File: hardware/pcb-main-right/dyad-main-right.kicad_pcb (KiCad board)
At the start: 2 copper layers, 167.2 x 120.7 mm, 148 parts, among them SW1 SW_Push, SW10 SW_Push, SW11 SW_Push, SW12 SW_Push, SW13 SW_Push, SW14 SW_Push, SW15 SW_Push, SW16 SW_Push, SW17 SW_Push, SW18 SW_Push, SW19 SW_Push, SW2 SW_Push, SW20 SW_Push, SW21 SW_Push, SW22 SW_Push, SW23 SW_Push, SW24 SW_Push, SW25 SW_Push, SW26 SW_Push, SW27 SW_Push, SW28 SW_Push, SW29 SW_Push, SW3 SW_Push, SW30 SW_Push, SW31 SW_Push, SW32 SW_Push, SW33 SW_Push, SW34 SW_Push, SW35 SW_Push, SW36 SW_Push, SW37 SW_Push, SW4 SW_Push, SW5 SW_Push, SW6 SW_Push, SW7 SW_Push, SW8 SW_Push, SW9 SW_Push

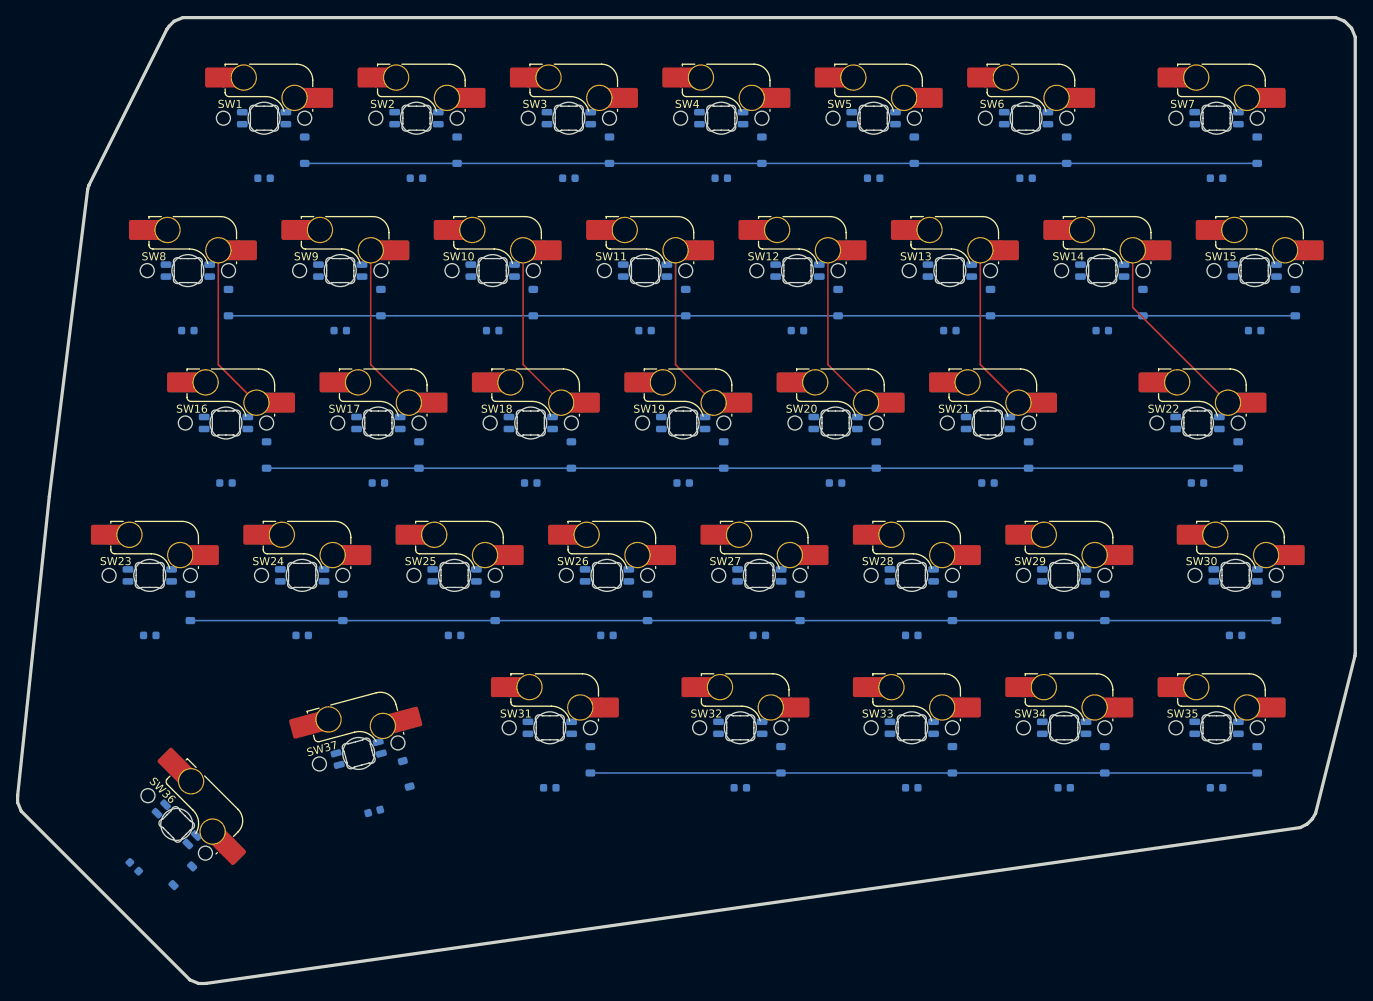
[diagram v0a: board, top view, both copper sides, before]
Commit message: Place switches on the back so hotswap sockets are on the underside
Caught in review: the sockets were on the same side as the switches.

marbastlib's hotswap footprint carries its socket pads on F.Cu and draws
its pin holes mirrored -- it is drawn as seen from underneath and must be
placed on the back. kbplacer defaults to front, so the sockets landed on
the switch side. Fixed with -s "SW{} 0 BACK"; stabilizers follow (they are
purely mechanical NPTH and X-symmetric, so flipping is a no-op for them).

Now every component is on the underside and switches insert from the top,
as a hotswap board should be. Verified: SW1's hotswap SMD pads are on
B.Cu, and the pin1->pin2 vector is (-6.35, 2.54), matching KiCad's stock
SW_Cherry_MX_1.00u_PCB. Absolute pad coordinates are not comparable
between the two libraries -- marbastlib's origin is the switch centre,
KiCad's is pin 1 -- so the vector is the valid test. An earlier claim in
this session that the geometry was mirrored wrongly was based on that bad
comparison and was itself wrong.

Also drops switch-to-diode routing failures, which were "no common layers
found" precisely because front-only SMD pads could not reach back-side
diodes.

DRC now runs and the boards are clearly a placement scaffold, not a
finished layout. Left: 1151 violations, 220 unconnected. Specific causes,
for the next pass:

- 128 hole_clearance: LEDs sit at the switch centre, 0.121 mm from the MX
  centre-post NPTH. The centre is where marbastlib puts its own combined
  MX+WS2812 footprint, but SK6812MINI-E is larger and fouls the post. LED
  offset needs rework.
- 128 copper_edge_clearance: the reverse-mount LED footprint's own cutout
  sits 0.35 mm from its pads against a 0.5 mm board rule. A board-setup
  constraint to relax, not a placement error.
- 192 shorting_items: diode pads overlapping switch through-holes after
  the flip, plus hotswap SMD pads left with no net, which points at an
  incomplete schematic-to-PCB netlist sync.
- Silk overlaps a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
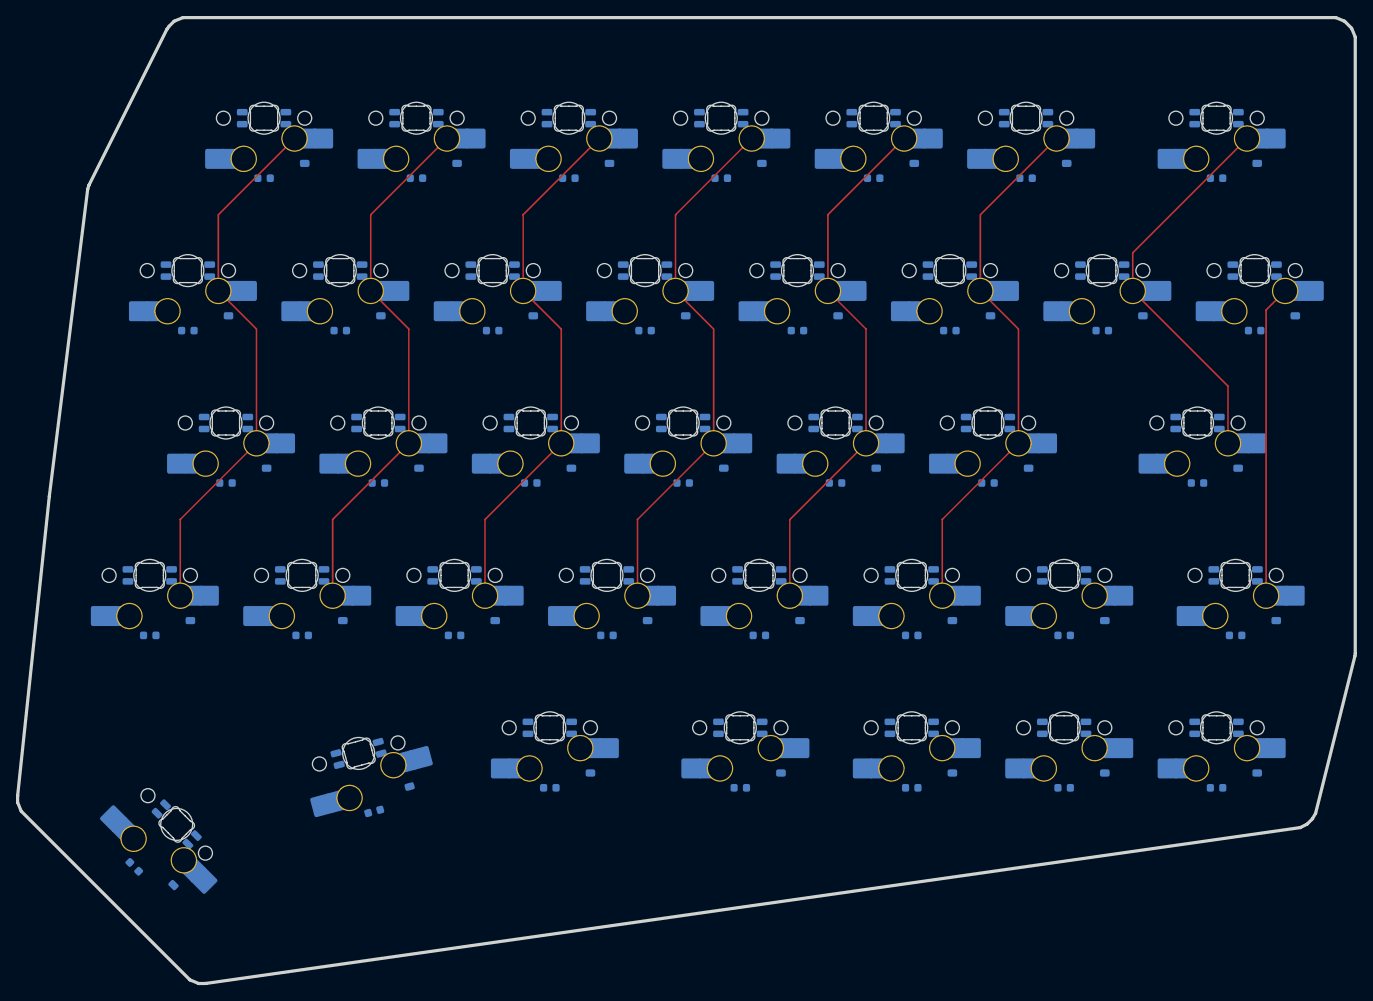
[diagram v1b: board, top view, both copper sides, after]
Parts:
- SW1, SW10, SW11, SW12, SW13, SW14, SW15, SW16, SW17, SW18, SW19, SW2, SW20, SW21, SW22, SW23, SW24, SW25, SW26, SW27, SW28, SW29, SW3, SW30, SW31, SW32, SW33, SW34, SW35, SW36, SW37, SW4, SW5, SW6, SW7, SW8, SW9: moved to B.Cu
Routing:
- net ROW3: track 135.7 -> 0.00 mm
- net ROW1: track 133.4 -> 0.00 mm
- net ROW2: track 121.4 -> 0.00 mm
- net ROW0: track 119.1 -> 0.00 mm
- net ROW4: track 83.3 -> 0.00 mm
- net COL4: track 21.0 -> 67.0 mm
- net COL3: track 21.0 -> 67.0 mm
- net COL2: track 21.0 -> 67.0 mm
- net COL1: track 21.0 -> 67.0 mm
- net COL0: track 21.0 -> 67.0 mm
- net COL5: track 21.0 -> 67.0 mm
- net COL7: track 0.00 -> 39.1 mm
- net COL6: track 24.0 -> 48.9 mm

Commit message: Fix LED offset and the placement errors it exposed
Working out the LED position turned up three further placement bugs.
Left board: 1151 -> 581 DRC violations, 220 -> 188 unconnected.

LED offset. ebastler's MX_SK6812MINI-E add-on -- a rear-mount SK6812MINI-E
for regular MX footprints -- puts its pads at y 4.33/5.83, centroid
(0, +5.08): 5.08 mm south of the switch centre, one fifth of an inch. Its
pad geometry matches KiCad's stock ReverseMount footprint almost exactly
(x +-2.6 vs +-2.73, same +-0.75 in y), so the maintained stock footprint
drops in at that offset. At the switch centre it fouled the MX centre-post
hole by 0.12 mm.

Switch rotation. The switches were 180 deg from convention: pins landed
SOUTH of centre, exactly where the LED goes. KiCad's stock MX footprint
puts them NORTH, at (+2.54,-5.08) and (-3.81,-2.54) relative to the
centre-post NPTH. An earlier commit asserted the geometry was correct on
the strength of the pin1->pin2 vector; that test cannot see this, because
a 180 deg rotation with swapped pin numbering preserves the vector.

Diode. kbplacer's default position assumes an unrotated switch, so it sat
beside the COLUMN pin, which the schematic does not wire it to. Moved
beside switch pin 2 and turned 180 deg so the anode rather than the ROW
pad faces the switch -- the ROW pad had been 0.035 mm from it.

Pad nets. marbastlib's hotswap footprint carries pad "1" three times, one
PTH and two SMD. kbplacer nets only one, so DRC saw each switch shorting
itself, 128 times per board. The generator now propagates nets across
same-numbered pads.

Also: min_copper_edge_clearance to 0.2 mm, since the reverse-mount LED
footprint's own light cutout sits 0.247 mm from its pads. Applied after
the board save, because saving rewrites the project file and silently
reverted it the first time.

Remaining, for a manual pass: roughly half the count is silkscreen
cosmetics and lib_footprint_issues (the libraries are referenced by
absolute path, so KiCad reports them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
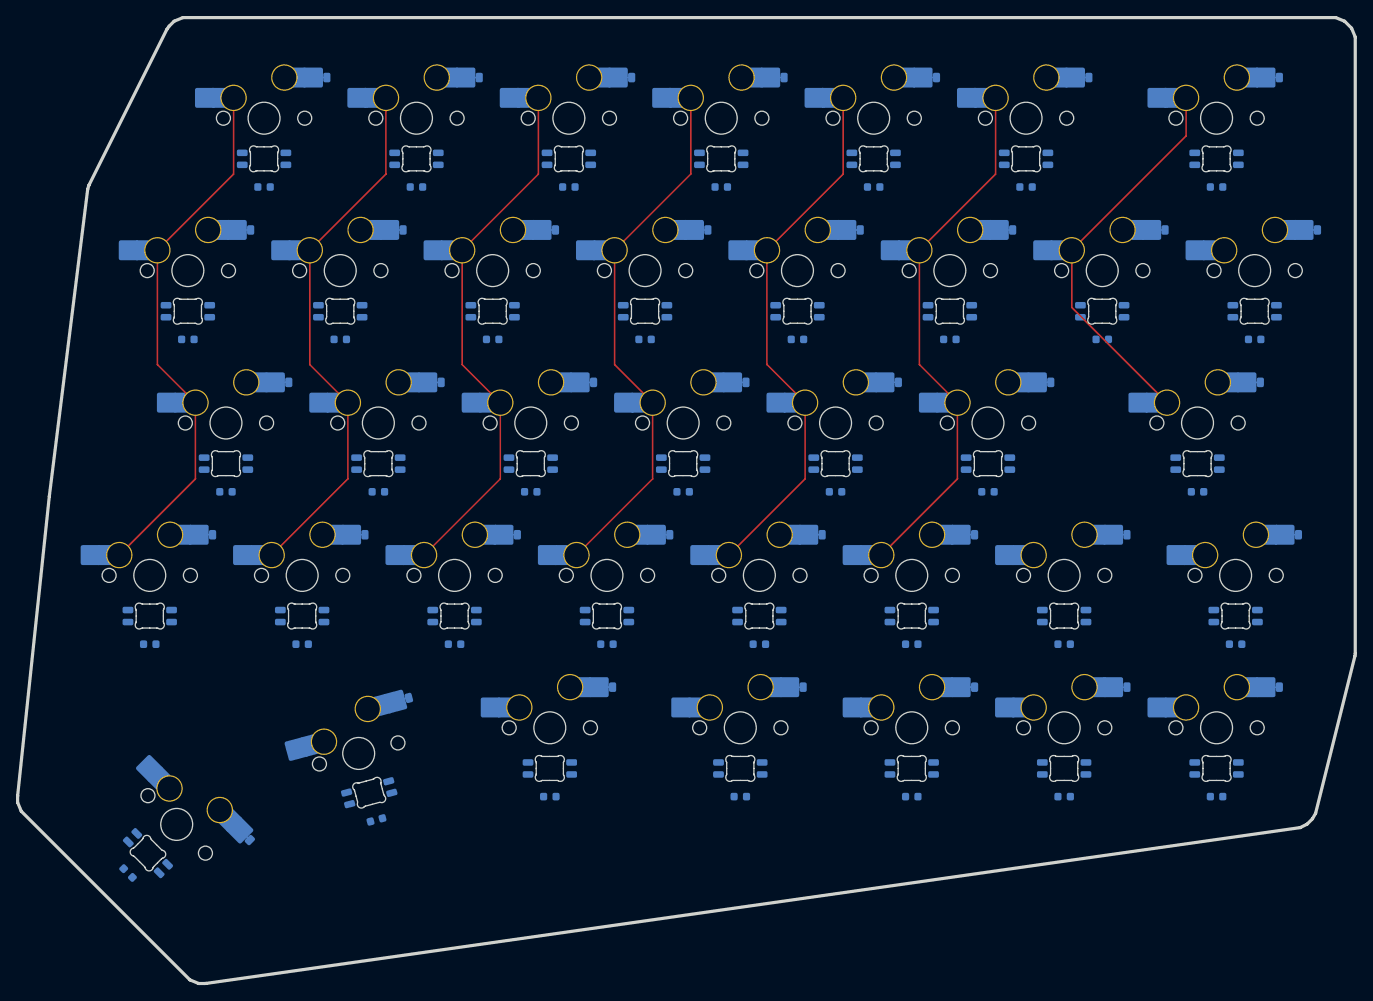
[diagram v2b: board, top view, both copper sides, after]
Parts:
- moved D36 9.15 mm to (54.2, 127.2), turned to -45 degrees
- moved D37 9.15 mm to (73.7, 111.0), turned to 15 degrees
- moved D1 9.15 mm to (63.4, 33.0), turned to 0 degrees
- moved D10 9.15 mm to (91.9, 52.1), turned to 0 degrees
- moved D11 9.15 mm to (111.0, 52.1), turned to 0 degrees
- moved D12 9.15 mm to (130.0, 52.1), turned to 0 degrees
- moved D14 9.15 mm to (168.1, 52.1), turned to 0 degrees
- moved D15 9.15 mm to (187.2, 52.1), turned to 0 degrees
- moved D16 9.15 mm to (58.6, 71.1), turned to 0 degrees
- moved D17 9.15 mm to (77.6, 71.1), turned to 0 degrees
- moved D18 9.15 mm to (96.7, 71.1), turned to 0 degrees
- moved D19 9.15 mm to (115.7, 71.1), turned to 0 degrees
- moved D2 9.15 mm to (82.4, 33.0), turned to 0 degrees
- moved D20 9.15 mm to (134.8, 71.1), turned to 0 degrees
- moved D21 9.15 mm to (153.8, 71.1), turned to 0 degrees
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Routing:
- net COL7: track 39.1 -> 0.00 mm
- net Net-(D33-A): track 0.00 -> 1.76 mm
- net Net-(D28-A): track 0.00 -> 1.76 mm
- net Net-(D22-A): track 0.00 -> 1.76 mm
- net Net-(D21-A): track 0.00 -> 1.76 mm
- net Net-(D14-A): track 0.00 -> 1.76 mm
- net Net-(D12-A): track 0.00 -> 1.76 mm
- net Net-(D32-A): track 0.00 -> 1.76 mm
- net Net-(D31-A): track 0.00 -> 1.76 mm
- net Net-(D25-A): track 0.00 -> 1.76 mm
- net Net-(D24-A): track 0.00 -> 1.76 mm
- net Net-(D19-A): track 0.00 -> 1.76 mm
- net Net-(D11-A): track 0.00 -> 1.76 mm
- net Net-(D10-A): track 0.00 -> 1.76 mm
- net Net-(D9-A): track 0.00 -> 1.76 mm
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
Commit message: Move the diode clear of the hotswap socket pads
Caught in review: the diode sat on top of a hotswap socket pad.

Confirmed in board coordinates -- the pad-2 socket SMD pads are at
(4.34,-5.08) and (6.09,-5.08), and the diode was at (6.20,-5.08),
directly on them.

Moved to (+8.40,-5.08) rotated 90 deg, as suggested. Position was solved
rather than estimated: the closest placement to the pad-2 socket it has to
reach, with at least 0.4 mm clearance to every pad of the switch, LED, cap
and the four neighbouring key cells. Achieves 0.43 mm clearance and a
2.3 mm route. Verified the anode faces the switch and the cathode carries
the ROW net.

Left board 581 -> 225 DRC violations. Four categories went to zero:
shorting_items, solder_mask_bridge, clearance, copper_edge_clearance.

What remains is largely not electrical: 96 silk_over_copper, 33
lib_footprint_issues (the libraries are referenced by absolute path, so
KiCad reports them as unconfigured), 32 silk_overlap and 32
silk_edge_clearance. The substantive remainder is 32 courtyards_overlap
between each diode and its switch, one track crossing an LED cutout on the
right board, and 188 nets still unrouted including the angled thumb keys.

The 2.25u stabilised key still needs manual attention -- the stabiliser is
not represented in the clearance model, and is being handled by hand.

Co-Authored-By: Claude Opus 5 <noreply@anthropic.com>
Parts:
- moved D37 2.20 mm to (75.8, 110.4), turned to -75 degrees
- moved D36 2.20 mm to (55.8, 128.7), turned to -135 degrees
- moved D13 2.20 mm to (151.3, 52.1), turned to -90 degrees
- moved D20 2.20 mm to (137.0, 71.1), turned to -90 degrees
- moved D30 2.20 mm to (187.0, 90.2), turned to -90 degrees
- moved D35 2.20 mm to (184.6, 109.2), turned to -90 degrees
- moved D6 2.20 mm to (160.8, 33.0), turned to -90 degrees
- moved D7 2.20 mm to (184.6, 33.0), turned to -90 degrees
- moved D10 2.20 mm to (94.1, 52.1), turned to -90 degrees
- moved D11 2.20 mm to (113.2, 52.1), turned to -90 degrees
- moved D16 2.20 mm to (60.8, 71.1), turned to -90 degrees
- moved D17 2.20 mm to (79.8, 71.1), turned to -90 degrees
- moved D18 2.20 mm to (98.9, 71.1), turned to -90 degrees
- moved D19 2.20 mm to (117.9, 71.1), turned to -90 degrees
- moved D23 2.20 mm to (51.3, 90.2), turned to -90 degrees
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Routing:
- net Net-(D35-A): track 1.76 -> 2.99 mm
- net Net-(D34-A): track 1.76 -> 2.99 mm
- net Net-(D30-A): track 1.76 -> 2.99 mm
- net Net-(D29-A): track 1.76 -> 2.99 mm
- net Net-(D27-A): track 1.76 -> 2.99 mm
- net Net-(D15-A): track 1.76 -> 2.99 mm
- net Net-(D13-A): track 1.76 -> 2.99 mm
- net Net-(D7-A): track 1.76 -> 2.99 mm
- net Net-(D6-A): track 1.76 -> 2.99 mm
- net Net-(D5-A): track 1.76 -> 2.99 mm
- net Net-(D3-A): track 1.76 -> 2.99 mm
- net Net-(D23-A): track 1.76 -> 2.99 mm
- net Net-(D9-A): track 1.76 -> 2.99 mm
- net Net-(D26-A): track 1.76 -> 2.99 mm
- net Net-(D20-A): track 1.76 -> 2.99 mm
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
